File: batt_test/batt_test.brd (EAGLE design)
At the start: 160 x 100 mm, 18 parts, among them J1 UART, U1 PHOTON

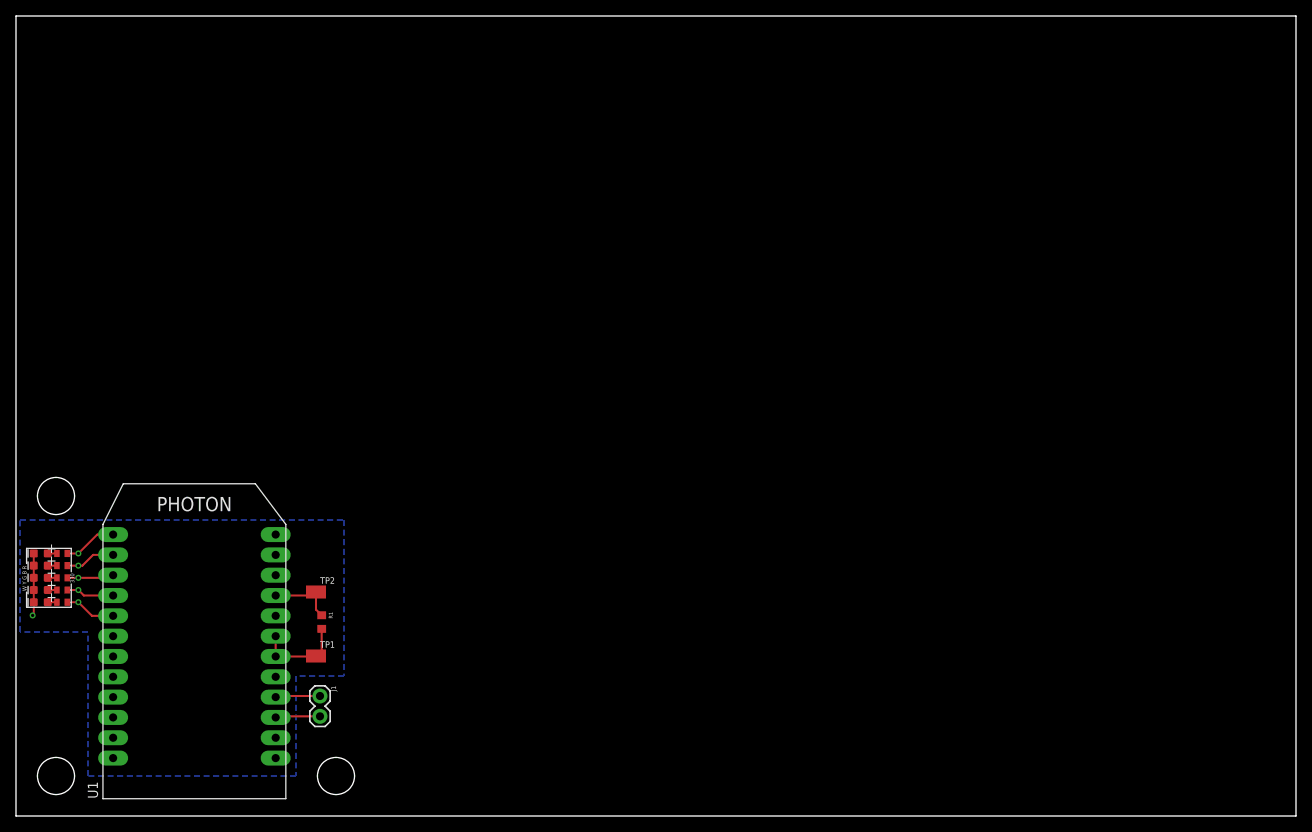
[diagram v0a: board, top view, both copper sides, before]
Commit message: add batt test point
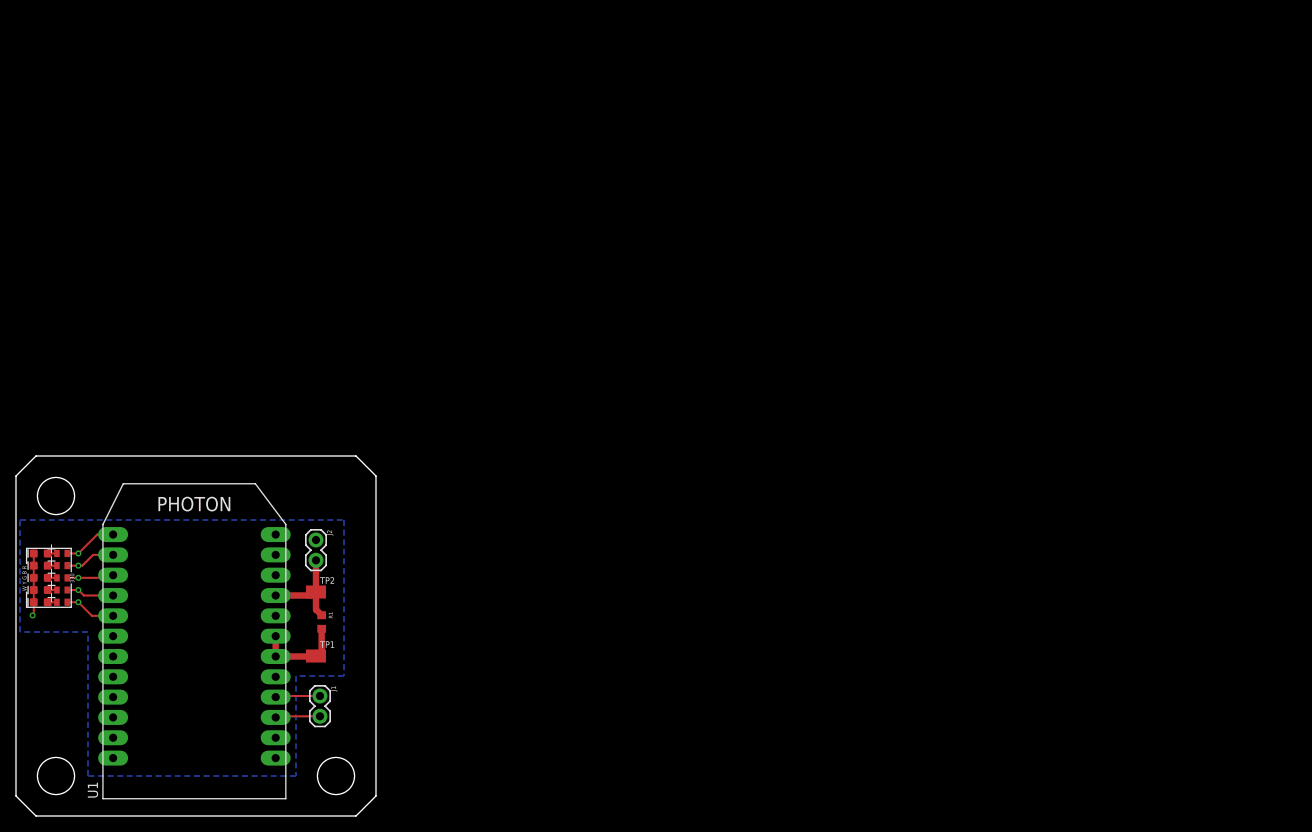
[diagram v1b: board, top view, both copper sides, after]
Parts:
- added J2: batt, scono:1X02
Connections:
- net B+: now also J2.2
- net GND: now also J2.1
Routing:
- net B+: track 8.43 -> 12.4 mm
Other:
- board size 160 x 100 mm -> 45 x 45 mm
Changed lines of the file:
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@@
 <board>
 <plain>
-<wire x1="0" y1="0" x2="160" y2="0" width="0" layer="20"/>
-<wire x1="160" y1="0" x2="160" y2="100" width="0" layer="20"/>
-<wire x1="160" y1="100" x2="0" y2="100" width="0" layer="20"/>
-<wire x1="0" y1="100" x2="0" y2="0" width="0" layer="20"/>
+<wire x1="0" y1="2.5" x2="2.5" y2="0" width="0" layer="20"/>
+<wire x1="2.5" y1="0" x2="42.5" y2="0" width="0" layer="20"/>
+<wire x1="42.5" y1="0" x2="45" y2="2.5" width="0" layer="20"/>
+<wire x1="45" y1="2.5" x2="45" y2="42.5" width="0" layer="20"/>
+<wire x1="45" y1="42.5" x2="42.5" y2="45" width="0" layer="20"/>
+<wire x1="42.5" y1="45" x2="2.5" y2="45" width="0" layer="20"/>
+<wire x1="2.5" y1="45" x2="0" y2="42.5" width="0" layer="20"/>
+<wire x1="0" y1="42.5" x2="0" y2="2.5" width="0" layer="20"/>
 <text x="7.289" y="29.135" size="0.508" layer="21" font="vector" rot="R90">330</text>
 <wire x1="6.908" y1="26.087" x2="1.32" y2="26.087" width="0.1524" layer="21"/>
@@
 <element name="U$2" library="scono" package="4-40-HOLE" value="" x="40" y="5" smashed="yes"/>
 <element name="U$3" library="scono" package="4-40-HOLE" value="" x="5" y="40" smashed="yes"/>
+<element name="J2" library="scono" package="1X02" package3d_urn="urn:adsk.eagle:package:38039/1" value="batt" x="37.5" y="34.5" smashed="yes" rot="R270">
+<attribute name="NAME" x="38.897" y="35.77" size="0.6096" layer="25" font="vector" ratio="20" rot="R270"/>
+<attribute name="VALUE" x="35.468" y="35.77" size="0.6096" layer="27" font="vector" ratio="20" rot="R270"/>
+</element>
 </elements>
 <signals>
@@
 <contactref element="U1" pad="DAC"/>
 <contactref element="TP1" pad="1"/>
-<wire x1="38.21" y1="23.39" x2="38.21" y2="20.71" width="0.254" layer="1"/>
+<wire x1="38.21" y1="23.39" x2="38.21" y2="20.71" width="0.8" layer="1"/>
 <wire x1="38.21" y1="20.71" x2="37.5" y2="20" width="0.254" layer="1"/>
 <wire x1="37.5" y1="20" x2="37.44" y2="19.94" width="0.254" layer="1"/>
-<wire x1="37.44" y1="19.94" x2="32.46" y2="19.94" width="0.254" layer="1"/>
-<wire x1="32.46" y1="19.94" x2="32.46" y2="22.48" width="0.254" layer="1"/>
+<wire x1="37.44" y1="19.94" x2="32.46" y2="19.94" width="0.8" layer="1"/>
+<wire x1="32.46" y1="19.94" x2="32.46" y2="22.48" width="0.8" layer="1"/>
 </signal>
 <signal name="B+">
@@
 <contactref element="U1" pad="A3"/>
 <contactref element="TP2" pad="1"/>
-<wire x1="32.46" y1="27.56" x2="37.06" y2="27.56" width="0.254" layer="1"/>
+<wire x1="32.46" y1="27.56" x2="37.06" y2="27.56" width="0.8" layer="1"/>
 <wire x1="37.06" y1="27.56" x2="37.5" y2="28" width="0.254" layer="1"/>
-<wire x1="37.5" y1="28" x2="37.5" y2="25.8" width="0.254" layer="1"/>
-<wire x1="37.5" y1="25.8" x2="38.21" y2="25.09" width="0.254" layer="1"/>
+<wire x1="37.5" y1="28" x2="37.5" y2="25.8" width="0.8" layer="1"/>
+<wire x1="37.5" y1="25.8" x2="38.21" y2="25.09" width="0.8" layer="1"/>
+<contactref element="J2" pad="2"/>
+<wire x1="37.5" y1="31.96" x2="37.5" y2="28" width="0.8" layer="1"/>
 </signal>
 <signal name="GND">
@@
 <vertex x="0.5" y="23"/>
 </polygon>
+<contactref element="J2" pad="1"/>
 </signal>
 <signal name="N$6">

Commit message: finish first proto
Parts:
- added B1: 2020COINCELL, scono:20MMCOINCELL
- added U$4: (no value), scono:4-40-HOLE
- moved J2 2.50 mm to (40.0, 34.5), turned to 180 degrees
- renumbered TP1 to B-, TP2 to POS
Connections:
- net B+: now also B1.POS
- net GND: now also B1.NEG
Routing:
- net B+: track 12.4 -> 30.7 mm
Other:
- board size 45 x 45 mm -> 50.5 x 45 mm
- board text added: "NEG"
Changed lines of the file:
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@@
 <wire x1="0" y1="2.5" x2="2.5" y2="0" width="0" layer="20"/>
 <wire x1="2.5" y1="0" x2="42.5" y2="0" width="0" layer="20"/>
-<wire x1="42.5" y1="0" x2="45" y2="2.5" width="0" layer="20"/>
-<wire x1="45" y1="2.5" x2="45" y2="42.5" width="0" layer="20"/>
-<wire x1="45" y1="42.5" x2="42.5" y2="45" width="0" layer="20"/>
+<wire x1="42.5" y1="0" x2="50.5" y2="2.5" width="0" layer="20"/>
+<wire x1="50.5" y1="2.5" x2="50.5" y2="42.5" width="0" layer="20"/>
+<wire x1="50.5" y1="42.5" x2="42.5" y2="45" width="0" layer="20"/>
 <wire x1="42.5" y1="45" x2="2.5" y2="45" width="0" layer="20"/>
 <wire x1="2.5" y1="45" x2="0" y2="42.5" width="0" layer="20"/>
@@
 <wire x1="1.32" y1="26.087" x2="1.32" y2="27.992" width="0.1524" layer="21"/>
 <wire x1="1.32" y1="33.453" x2="1.32" y2="31.548" width="0.1524" layer="21"/>
-<text x="7" y="10" size="1" layer="27" font="vector" rot="R90">Arias Research Group
+<text x="7" y="10" size="1" layer="21" font="vector" rot="R90">Arias Research Group
 Board Design - S. Ono
 Battery Testing Board</text>
+<text x="41.5" y="36" size="0.8" layer="21" font="vector" align="bottom-right">NEG</text>
 </plain>
 <attributes>
@@
 </class>
 </classes>
-<designrules name="scono">
+<designrules name="scono *">
 <description language="de">&lt;b&gt;EAGLE Design Rules&lt;/b&gt;
 &lt;p&gt;
@@
 <param name="msMicroVia" value="9.99mm"/>
 <param name="msBlindViaRatio" value="0.125"/>
-<param name="rvPadTop" value="0.1"/>
+<param name="rvPadTop" value="0.25"/>
 <param name="rvPadInner" value="0.1"/>
-<param name="rvPadBottom" value="0.1"/>
+<param name="rvPadBottom" value="0.25"/>
 <param name="rvViaOuter" value="0.25"/>
 <param name="rvViaInner" value="0.25"/>
@@
 <attribute name="VALUE" x="4.622" y="31.548" size="0.508" layer="27" font="vector"/>
 </element>
-<element name="TP1" library="scono" package="TEST_POINT-1206" value="TEST_POINT" x="37.5" y="20" smashed="yes">
+<element name="B-" library="scono" package="TEST_POINT-1206" value="TEST_POINT" x="37.5" y="20" smashed="yes">
 <attribute name="NAME" x="39.87" y="21.84" size="0.8128" layer="25" font="vector" rot="R180"/>
 </element>
-<element name="TP2" library="scono" package="TEST_POINT-1206" value="TEST_POINT" x="37.5" y="28" smashed="yes">
-<attribute name="NAME" x="39.87" y="29.84" size="0.8128" layer="25" font="vector" rot="R180"/>
+<element name="POS" library="scono" package="TEST_POINT-1206" value="TEST_POINT" x="37.5" y="28" smashed="yes">
+<attribute name="NAME" x="36" y="36" size="0.8" layer="25" font="vector"/>
 </element>
 <element name="J1" library="scono" package="1X02" package3d_urn="urn:adsk.eagle:package:38039/1" value="UART" x="38" y="15" smashed="yes" rot="R270">
@@
 <element name="U$2" library="scono" package="4-40-HOLE" value="" x="40" y="5" smashed="yes"/>
 <element name="U$3" library="scono" package="4-40-HOLE" value="" x="5" y="40" smashed="yes"/>
-<element name="J2" library="scono" package="1X02" package3d_urn="urn:adsk.eagle:package:38039/1" value="batt" x="37.5" y="34.5" smashed="yes" rot="R270">
-<attribute name="NAME" x="38.897" y="35.77" size="0.6096" layer="25" font="vector" ratio="20" rot="R270"/>
-<attribute name="VALUE" x="35.468" y="35.77" size="0.6096" layer="27" font="vector" ratio="20" rot="R270"/>
-</element>
+<element name="J2" library="scono" package="1X02" package3d_urn="urn:adsk.eagle:package:38039/1" value="batt" x="40" y="34.5" smashed="yes" rot="R180">
+<attribute name="NAME" x="41.27" y="33.103" size="0.6096" layer="25" font="vector" ratio="20" rot="R180"/>
+</element>
+<element name="B1" library="scono" package="20MMCOINCELL" value="2020COINCELL" x="47" y="28" smashed="yes" rot="R90">
+<attribute name="NAME" x="43" y="14" size="0.7" layer="25" font="vector" rot="R90"/>
+</element>
+<element name="U$4" library="scono" package="4-40-HOLE" value="" x="40" y="40" smashed="yes"/>
 </elements>
 <signals>
@@
 <contactref element="U1" pad="A5"/>
 <contactref element="U1" pad="DAC"/>
-<contactref element="TP1" pad="1"/>
+<contactref element="B-" pad="1"/>
 <wire x1="38.21" y1="23.39" x2="38.21" y2="20.71" width="0.8" layer="1"/>
 <wire x1="38.21" y1="20.71" x2="37.5" y2="20" width="0.254" layer="1"/>
@@
 <contactref element="R1" pad="1"/>
 <contactref element="U1" pad="A3"/>
-<contactref element="TP2" pad="1"/>
+<contactref element="POS" pad="1"/>
 <wire x1="32.46" y1="27.56" x2="37.06" y2="27.56" width="0.8" layer="1"/>
 <wire x1="37.06" y1="27.56" x2="37.5" y2="28" width="0.254" layer="1"/>
@@
 <wire x1="37.5" y1="25.8" x2="38.21" y2="25.09" width="0.8" layer="1"/>
 <contactref element="J2" pad="2"/>
-<wire x1="37.5" y1="31.96" x2="37.5" y2="28" width="0.8" layer="1"/>
+<contactref element="B1" pad="POS"/>
+<wire x1="38.21" y1="25.09" x2="41.41" y2="25.09" width="0.8" layer="1"/>
+<wire x1="41.41" y1="25.09" x2="42.5" y2="24" width="0.8" layer="1"/>
+<wire x1="42.5" y1="24" x2="42.5" y2="19.419" width="0.8" layer="1"/>
+<wire x1="42.5" y1="19.419" x2="47" y2="14.919" width="0.8" layer="1"/>
+<wire x1="37.5" y1="28" x2="37.46" y2="28" width="0.8" layer="1"/>
+<wire x1="37.46" y1="28" x2="37.46" y2="34.5" width="0.8" layer="1"/>
 </signal>
 <signal name="GND">
@@
 <polygon width="0.1524" layer="16">
 <vertex x="0.5" y="37"/>
-<vertex x="41" y="37"/>
+<vertex x="44" y="37"/>
+<vertex x="44" y="31"/>
+<vertex x="46" y="31"/>
+<vertex x="46" y="26"/>
+<vertex x="41" y="26"/>
 <vertex x="41" y="17.5"/>
 <vertex x="35" y="17.5"/>
@@
 </polygon>
 <contactref element="J2" pad="1"/>
+<contactref element="B1" pad="NEG"/>
 </signal>
 <signal name="N$6">

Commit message: update bom and gerber
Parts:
- removed J1: UART, scono:1X02
- removed J2: batt, scono:1X02
- removed U$2: (no value), scono:4-40-HOLE
- added B+, TP2: TEST_POINTTHRU, scono:TEST_POINT
- added U2: 1101M2S3CQE2, scono:1101M2S3CQE2
- moved B- 0.50 mm to (37.5, 19.5)
- moved B1 0.50 mm to (47.0, 27.5)
- moved D1 0.50 mm to (3.10, 26.2)
- moved D3 0.50 mm to (3.10, 27.7)
- moved D4 0.50 mm to (3.10, 29.3)
- moved D5 0.50 mm to (3.10, 30.8)
- moved D6 0.50 mm to (3.10, 32.3)
- moved POS 0.50 mm to (37.5, 27.5)
- moved R1 0.50 mm to (38.2, 23.7)
- moved R2 0.50 mm to (5.76, 26.2)
- moved R3 0.50 mm to (5.76, 27.7)
- moved R4 0.50 mm to (5.76, 29.3)
- moved R5 0.50 mm to (5.76, 30.8)
- moved R6 0.50 mm to (5.76, 32.3)
- moved U$3 0.50 mm to (5.00, 39.5)
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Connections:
- removed net RX: J1.1, U1.RX
- removed net TX: J1.2, U1.TX
- new net N$1: B1.NEG, U2.1
- net B+: now also B+.1; no longer J2.2
- net GND: now also TP2.1, U2.2; no longer B1.NEG, J2.1
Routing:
- net B+: track 30.7 -> 49.6 mm
- net N$1: track 0.00 -> 15.4 mm
- net TX: track 5.60 -> 0.00 mm
- net RX: track 5.60 -> 0.00 mm
- net YELLOW: track 6.28 -> 7.55 mm
- net WHITE: track 6.70 -> 7.97 mm
- net RED: track 6.43 -> 7.70 mm
- net GREEN: track 5.86 -> 7.13 mm
- net BLUE: track 6.01 -> 7.28 mm
- net B-: track 11.3 -> 12.6 mm
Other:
- board size 50.5 x 45 mm -> 50.5 x 44.5 mm
- board text added: "GND"
- board text added: "OFF"
- board text added: "ON"
- board text added: "POS"
